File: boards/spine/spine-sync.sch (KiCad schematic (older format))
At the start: 6 parts, among them CON3 PLR135, CON4 PLT133

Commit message: BOM cleanup
Especially fix the confusing and mostly incorrect Mfg/Mfr stuff that I inherited from somewhere.
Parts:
- C81, C82: Mfg1 (none) -> Murata; Mfg1Id (none) -> GRM21BR71H104MA01L; MfgId GRM21BR71H104MA01L -> (none); MfrId Murata -> (none)
- C83: Mfg1 (none) -> Murata; Mfg1Id (none) -> GRM219R61H105KA73D; MfgId GRM219R61H105KA73D -> (none); MfrId Murata -> (none)
- CON3: Mfg1 (none) -> Everlight; Mfg1Id (none) -> PLR135/T10; MfgId PLR135/T10 -> (none); MfrId Everlight -> (none)
- CON4: Mfg1 (none) -> Everlight; Mfg1Id (none) -> PLT133/T; MfgId PLT133/T -> (none); MfrId Everlight -> (none)
- FB7: Mfg1 (none) -> Samsung; Mfg1Id (none) -> CIS21P300NE; MfgId CIS21P300NE -> (none); MfrId Samsung -> (none)
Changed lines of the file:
@@
 F 4 "Digikey" H 5900 3100 60  0001 C CNN "Vend1"
 F 5 "1080-1428-ND" H 5900 3100 60  0001 C CNN "Vend1Id"
-F 6 "Everlight" H 5900 3100 60  0001 C CNN "MfrId"
-F 7 "PLT133/T" H 5900 3100 60  0001 C CNN "MfgId"
+F 6 "Everlight" H 5900 3100 60  0001 C CNN "Mfg1"
+F 7 "PLT133/T" H 5900 3100 60  0001 C CNN "Mfg1Id"
 F 8 "0.37125" H 5900 3100 60  0001 C CNN "RefPrice1k"
 	1    5900 3100
@@
 F 5 "490-9672-2-ND" V 4750 3100 60  0001 C CNN "Vend1Id"
 F 6 "Digikey" V 4750 3100 60  0001 C CNN "Vend1"
-F 7 "Murata" V 4750 3100 60  0001 C CNN "MfrId"
-F 8 "GRM21BR71H104MA01L" V 4750 3100 60  0001 C CNN "MfgId"
+F 7 "Murata" V 4750 3100 60  0001 C CNN "Mfg1"
+F 8 "GRM21BR71H104MA01L" V 4750 3100 60  0001 C CNN "Mfg1Id"
 	1    4750 3100
 	-1   0    0    1
@@
 F 5 "1080-1433-ND" H 4800 5100 60  0001 C CNN "Vend1Id"
 F 6 "0.73054" H 4800 5100 60  0001 C CNN "RefPrice1k"
-F 7 "Everlight" H 4800 5100 60  0001 C CNN "MfrId"
-F 8 "PLR135/T10" H 4800 5100 60  0001 C CNN "MfgId"
+F 7 "Everlight" H 4800 5100 60  0001 C CNN "Mfg1"
+F 8 "PLR135/T10" H 4800 5100 60  0001 C CNN "Mfg1Id"
 	1    4800 5100
 	1    0    0    -1
@@
 F 5 "490-9672-2-ND" V 6050 5100 60  0001 C CNN "Vend1Id"
 F 6 "Digikey" V 6050 5100 60  0001 C CNN "Vend1"
-F 7 "Murata" V 6050 5100 60  0001 C CNN "MfrId"
-F 8 "GRM21BR71H104MA01L" V 6050 5100 60  0001 C CNN "MfgId"
+F 7 "Murata" V 6050 5100 60  0001 C CNN "Mfg1"
+F 8 "GRM21BR71H104MA01L" V 6050 5100 60  0001 C CNN "Mfg1Id"
 	1    6050 5100
 	-1   0    0    1
@@
 F 3 "http://www.samsungsem.com/kr/front/downloadcms.do?path=/kr/support/product-search/bead/__icsFiles/afieldfile/2014/11/13&fileName=S_CIS21J121NE.pdf" H 6075 4400 60  0001 C CNN
 F 4 "0.02383" H 6050 4400 60  0001 C CNN "RefPrice1k"
-F 5 "Samsung" H 6050 4400 60  0001 C CNN "MfrId"
-F 6 "CIS21P300NE" H 6050 4400 60  0001 C CNN "MfgId"
+F 5 "Samsung" H 6050 4400 60  0001 C CNN "Mfg1"
+F 6 "CIS21P300NE" H 6050 4400 60  0001 C CNN "Mfg1Id"
 F 7 "Digikey" H 6050 4400 60  0001 C CNN "Vend1"
 F 8 "1276-6370-1-ND" H 6050 4400 60  0001 C CNN "Vend1Id"
@@
 F 2 "Capacitors_SMD:C_0805" H 6488 4950 30  0001 C CNN
 F 3 "http://www.murata.com/~/media/webrenewal/support/library/catalog/products/capacitor/mlcc/c02e.ashx" H 6450 5100 60  0001 C CNN
-F 4 "GRM219R61H105KA73D" H 6500 4900 39  0001 L BNN "MfgId"
-F 5 "Murata" H 6450 5100 60  0001 C CNN "MfrId"
+F 4 "GRM219R61H105KA73D" H 6500 4900 39  0001 L BNN "Mfg1Id"
+F 5 "Murata" H 6450 5100 60  0001 C CNN "Mfg1"
 F 6 "Digikey" H 6450 5100 60  0001 C CNN "Vend1"
 F 7 "490-10743-2-ND" H 6450 5100 60  0001 C CNN "Vend1Id"

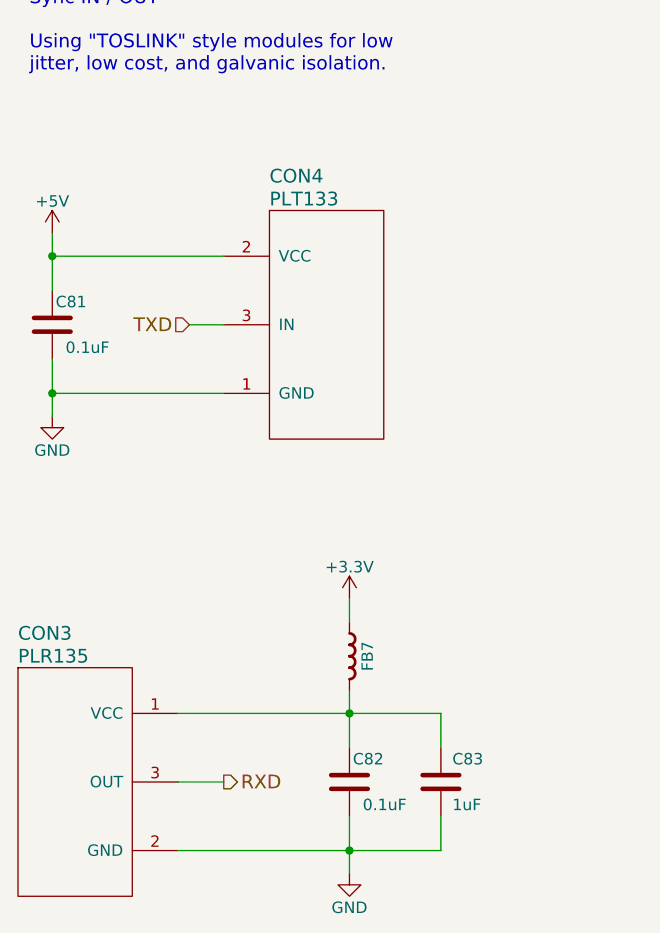
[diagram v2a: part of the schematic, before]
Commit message: Capacitor upgrades, BOM tidying
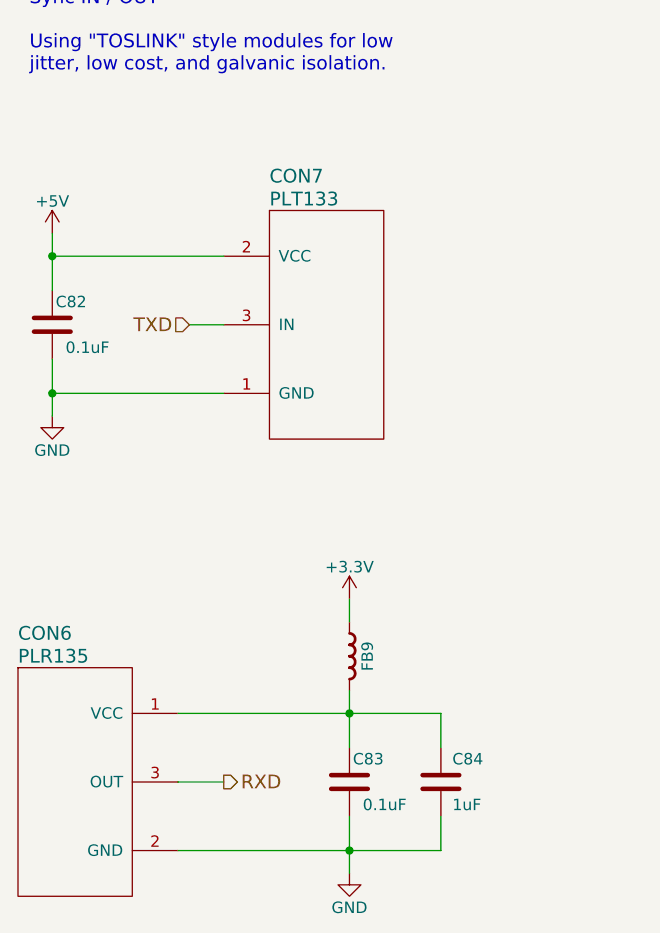
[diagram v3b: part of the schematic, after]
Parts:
- renumbered C81 to C82, C82 to C83, C83 to C84, CON3 to CON6, CON4 to CON7, FB7 to FB9
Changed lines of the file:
@@
 TXD
 $Comp
-L PLT133/T CON4
+L PLT133/T CON7
 U 1 1 5650BE58
 P 5900 3100
-F 0 "CON4" H 5700 3750 60  0000 L CNN
+F 0 "CON7" H 5700 3750 60  0000 L CNN
 F 1 "PLT133" H 5700 3650 60  0000 L CNN
 F 2 "TOSLINK:Everlight-PLT133-T6A" H 5900 4000 60  0001 C CNN
@@
 	5500 3100 5350 3100
 $Comp
-L C C81
+L C C82
 U 1 1 5650C7E8
 P 4750 3100
-F 0 "C81" H 4600 3000 50  0000 L CNN
+F 0 "C82" H 4600 3000 50  0000 L CNN
 F 1 "0.1uF" H 4500 3200 50  0000 L CNN
 F 2 "Capacitors_SMD:C_0805" H 4788 2950 30  0001 C CNN
@@
 $EndComp
 $Comp
-L GND #PWR0159
+L GND #PWR170
 U 1 1 5650C9B4
 P 4750 3500
-F 0 "#PWR0159" H 4750 3250 50  0001 C CNN
+F 0 "#PWR170" H 4750 3250 50  0001 C CNN
 F 1 "GND" H 4750 3350 50  0000 C CNN
 F 2 "" H 4750 3500 60  0000 C CNN
@@
 $EndComp
 $Comp
-L +5V #PWR0160
+L +5V #PWR169
 U 1 1 5650C9FA
 P 4750 2700
-F 0 "#PWR0160" H 4750 2550 50  0001 C CNN
+F 0 "#PWR169" H 4750 2550 50  0001 C CNN
 F 1 "+5V" H 4750 2840 50  0000 C CNN
 F 2 "" H 4750 2700 60  0000 C CNN
@@
 Connection ~ 4750 2800
 $Comp
-L PLR135 CON3
+L PLR135 CON6
 U 1 1 5650E1F3
 P 4800 5100
-F 0 "CON3" H 4600 5750 60  0000 L CNN
+F 0 "CON6" H 4600 5750 60  0000 L CNN
 F 1 "PLR135" H 4600 5650 60  0000 L CNN
 F 2 "TOSLINK:Everlight-PLR135-T8" H 4800 6000 60  0001 C CNN
@@
 $EndComp
 $Comp
-L +3.3V #PWR0161
+L +3.3V #PWR171
 U 1 1 5650E21A
 P 6050 4300
-F 0 "#PWR0161" H 6050 4150 50  0001 C CNN
+F 0 "#PWR171" H 6050 4150 50  0001 C CNN
 F 1 "+3.3V" H 6050 4440 50  0000 C CNN
 F 2 "" H 6050 4300 60  0000 C CNN
@@
 $EndComp
 $Comp
-L C C82
+L C C83
 U 1 1 5650E26F
 P 6050 5100
-F 0 "C82" H 5900 5000 50  0000 L CNN
+F 0 "C83" H 5900 5000 50  0000 L CNN
 F 1 "0.1uF" H 5800 5200 50  0000 L CNN
 F 2 "Capacitors_SMD:C_0805" H 6088 4950 30  0001 C CNN
@@
 $EndComp
 $Comp
-L GND #PWR0162
+L GND #PWR172
 U 1 1 5650E275
 P 6050 5500
-F 0 "#PWR0162" H 6050 5250 50  0001 C CNN
+F 0 "#PWR172" H 6050 5250 50  0001 C CNN
 F 1 "GND" H 6050 5350 50  0000 C CNN
 F 2 "" H 6050 5500 60  0000 C CNN
@@
 	5300 4800 6450 4800
 $Comp
-L FERRITE_BEAD FB7
+L FERRITE_BEAD FB9
 U 1 1 5650F03C
 P 6050 4400
-F 0 "FB7" H 6200 4450 50  0000 C BNN
+F 0 "FB9" H 6200 4450 50  0000 C BNN
 F 1 "Ferrite bead" H 6450 4450 39  0001 C BNN
 F 2 "Resistors_SMD:R_0805" H 6050 4550 50  0001 C CNN
@@
 $EndComp
 $Comp
-L C C83
+L C C84
 U 1 1 5650F041
 P 6450 5100
-F 0 "C83" H 6500 5200 50  0000 L CNN
+F 0 "C84" H 6500 5200 50  0000 L CNN
 F 1 "1uF " H 6500 5000 50  0000 L CNN
 F 2 "Capacitors_SMD:C_0805" H 6488 4950 30  0001 C CNN
@@
 FB 59 00 E6 A5 69 3A 37 9E CF 73 BC F7 37 E3 33 5D 9E A8 3E 7F 80 FA F7 F6 BB 44 F4 6E D4 E7 77
 A2 1E 1F 27 A2 E3 16 70 32 E9 54 FE 3F E7 AF 00 CA 1C A3 36 0A 00 00 00 00 49 45 4E 44 AE 42 60
-82 00
+82 70
 EndData
 $EndBitmap

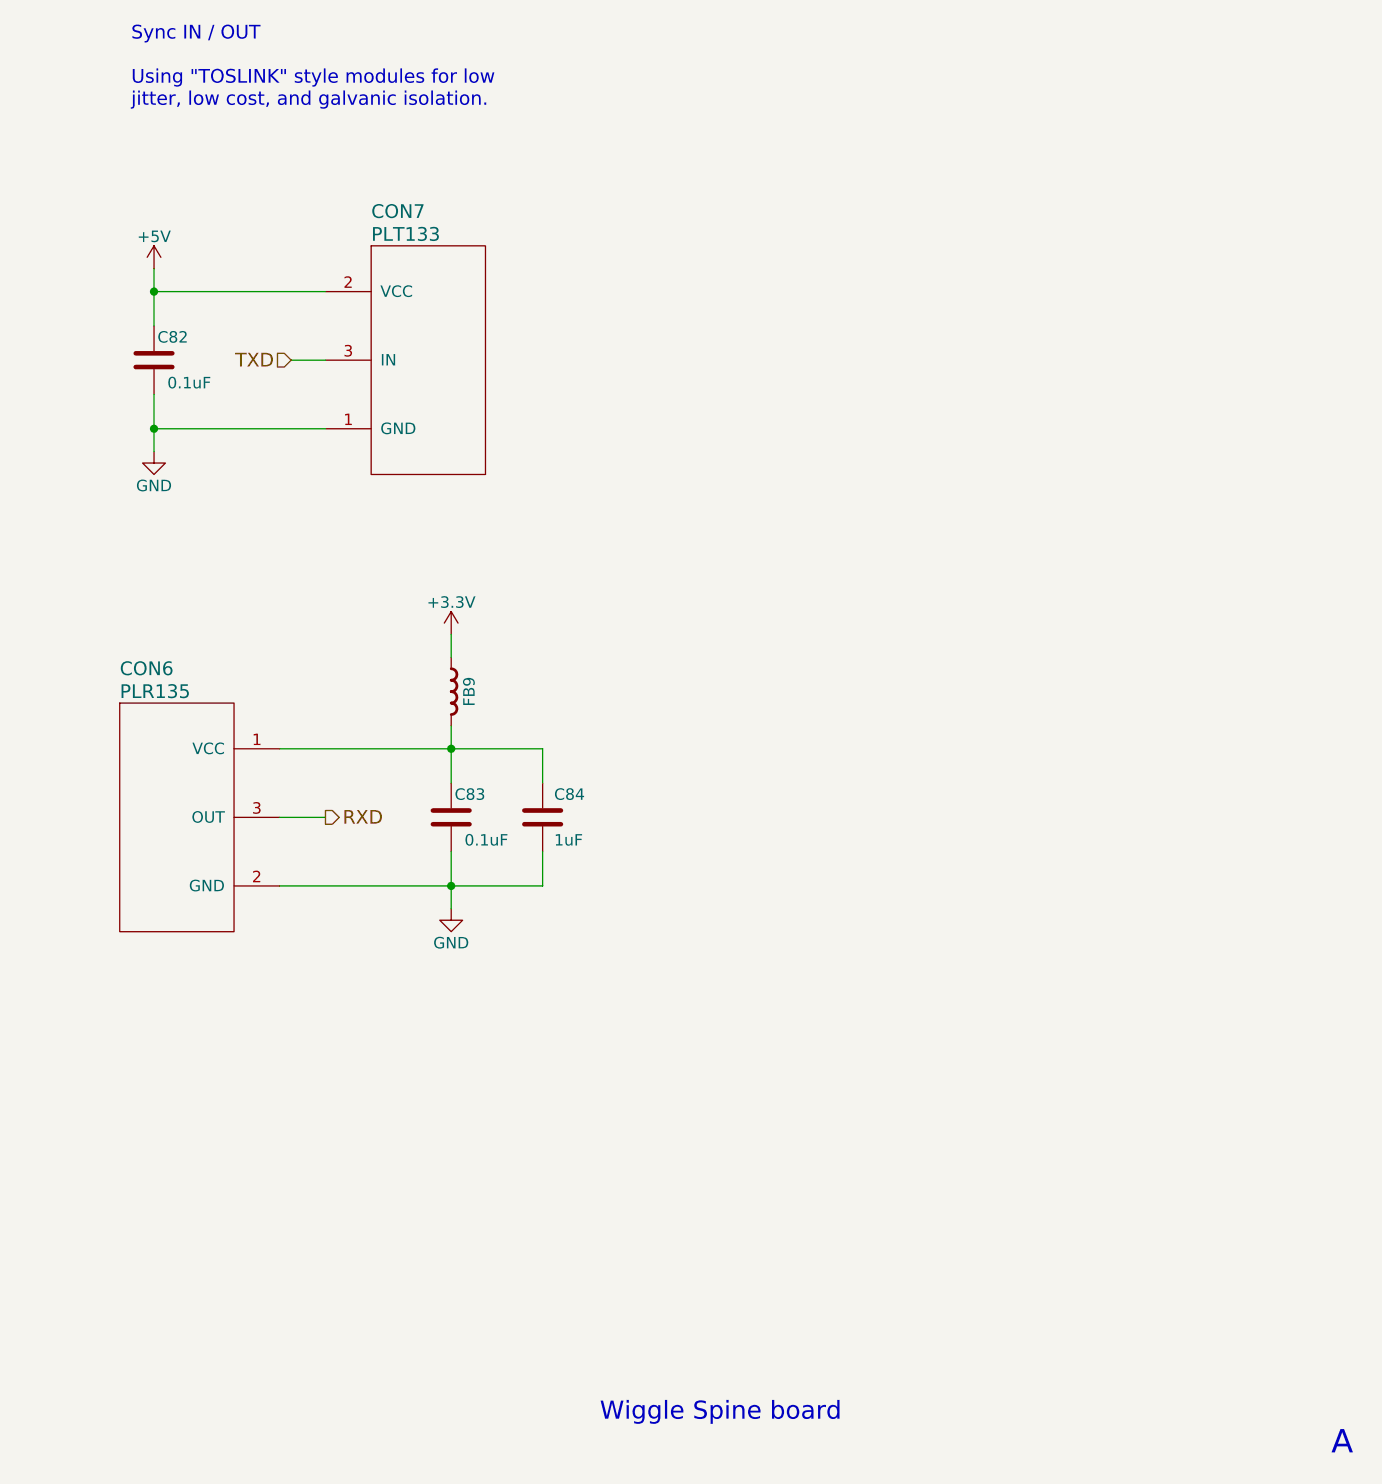
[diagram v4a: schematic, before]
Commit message: Schematics stabilizing for next proto, starting PCB updates
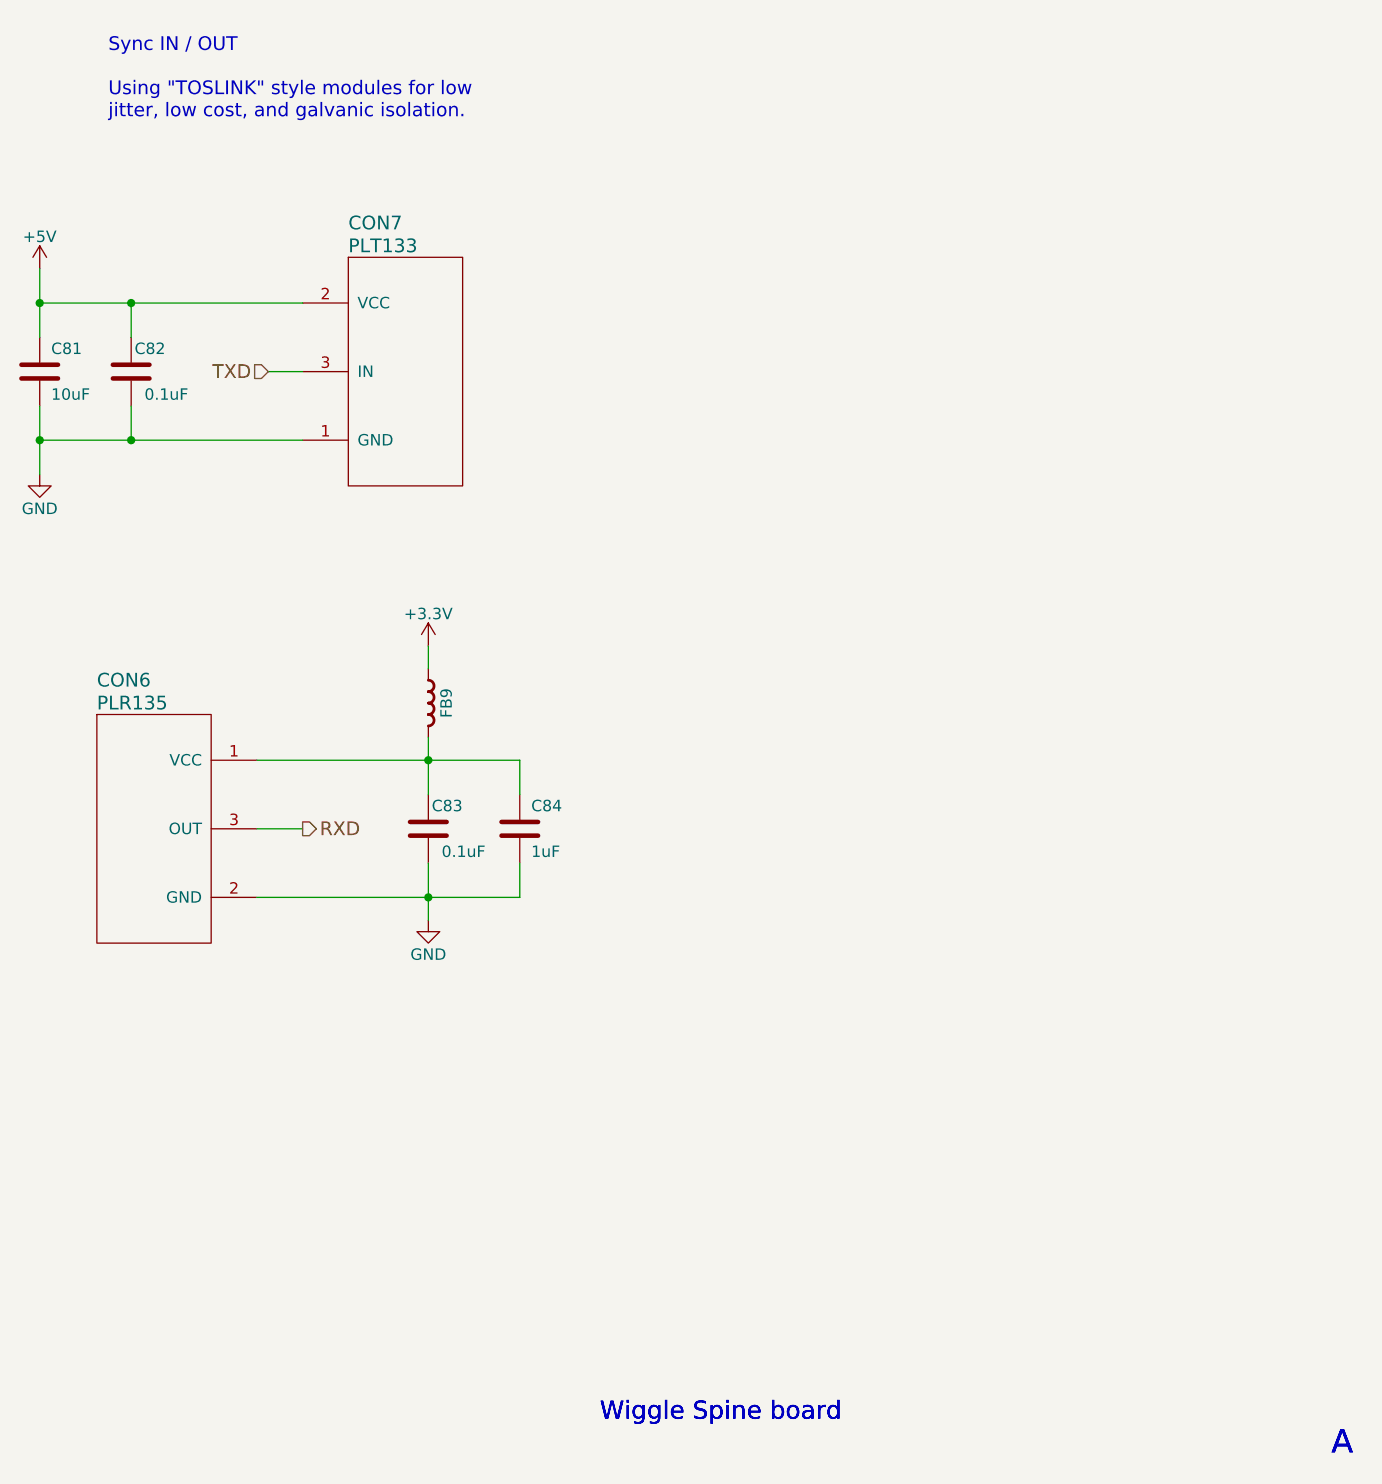
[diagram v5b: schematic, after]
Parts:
- added C81: 10uF, Capacitors_SMD:C_1206, symbol C
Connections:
- net +5V: now also C81.1
- net GND: now also C81.2
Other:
- moved on the sheet: C82, C83, C84, CON6, CON7, FB9
